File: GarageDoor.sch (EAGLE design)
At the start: 18 parts

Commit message: I hate git
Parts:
- added IC1: 7805DT, linear:7805DT
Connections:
- net GND: now also IC1.GND
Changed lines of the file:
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@@
 <part name="P+2" library="supply1" deviceset="+5V" device=""/>
 <part name="SUPPLY6" library="supply2" deviceset="GND" device=""/>
+<part name="SUPPLY7" library="supply2" deviceset="GND" device=""/>
+<part name="IC1" library="linear" deviceset="78*" device="DT" technology="05"/>
 </parts>
 <sheets>
@@
 <instance part="P+2" gate="1" x="213.36" y="38.1"/>
 <instance part="SUPPLY6" gate="GND" x="213.36" y="17.78"/>
+<instance part="SUPPLY7" gate="GND" x="-109.22" y="35.56"/>
+<instance part="IC1" gate="A1" x="-109.22" y="50.8"/>
 </instances>
 <busses>
@@
 <wire x1="213.36" y1="25.4" x2="213.36" y2="20.32" width="0.1524" layer="91"/>
 </segment>
+<segment>
+<pinref part="SUPPLY7" gate="GND" pin="GND"/>
+<wire x1="-109.22" y1="38.1" x2="-109.22" y2="43.18" width="0.1524" layer="91"/>
+<pinref part="IC1" gate="A1" pin="GND"/>
+</segment>
 </net>

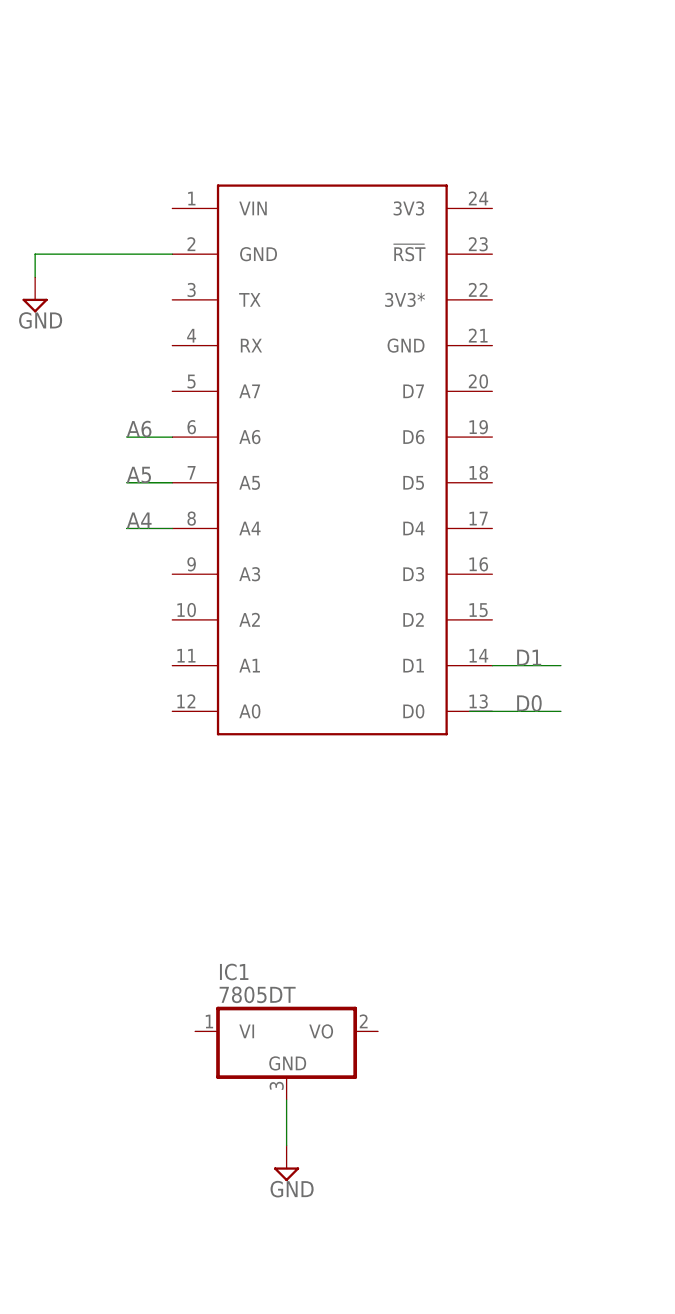
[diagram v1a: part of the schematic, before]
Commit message: 5V Regulator
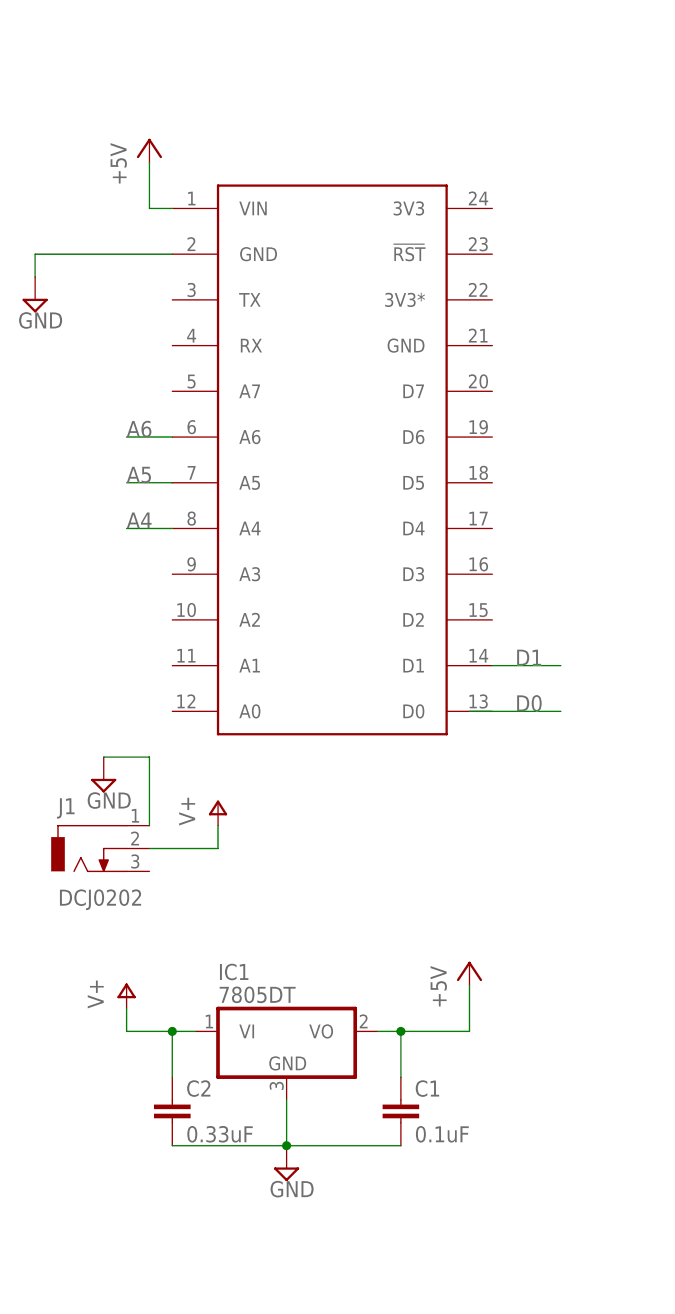
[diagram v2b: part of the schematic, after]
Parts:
- added C1: 0.1uF, rcl:C-EUC0805K
- added C2: 0.33uF, rcl:C-EUC0805K
- added J1: DCJ0202, con-jack:DCJ0202
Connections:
- new net V+: C2.1, IC1.VI, J1.2
- net +5V: now also C1.1, IC1.VO, U$1.VIN
- net GND: now also C1.2, C2.2, J1.1
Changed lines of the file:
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@@
 <part name="SUPPLY7" library="supply2" deviceset="GND" device=""/>
 <part name="IC1" library="linear" deviceset="78*" device="DT" technology="05"/>
+<part name="C1" library="rcl" deviceset="C-EU" device="C0805K" value="0.1uF"/>
+<part name="C2" library="rcl" deviceset="C-EU" device="C0805K" value="0.33uF"/>
+<part name="P+3" library="supply1" deviceset="+5V" device=""/>
+<part name="P+4" library="supply1" deviceset="+5V" device=""/>
+<part name="J1" library="con-jack" deviceset="DCJ0202" device=""/>
+<part name="P+5" library="supply1" deviceset="V+" device=""/>
+<part name="P+6" library="supply1" deviceset="V+" device=""/>
+<part name="SUPPLY8" library="supply2" deviceset="GND" device=""/>
 </parts>
 <sheets>
@@
 <instance part="SUPPLY7" gate="GND" x="-109.22" y="35.56"/>
 <instance part="IC1" gate="A1" x="-109.22" y="50.8"/>
+<instance part="C1" gate="G$1" x="-96.52" y="43.18"/>
+<instance part="C2" gate="G$1" x="-121.92" y="43.18"/>
+<instance part="P+3" gate="1" x="-124.46" y="149.86"/>
+<instance part="P+4" gate="1" x="-88.9" y="58.42"/>
+<instance part="J1" gate="G$1" x="-132.08" y="71.12"/>
+<instance part="P+5" gate="1" x="-116.84" y="76.2"/>
+<instance part="P+6" gate="1" x="-127" y="55.88"/>
+<instance part="SUPPLY8" gate="GND" x="-129.54" y="78.74"/>
 </instances>
 <busses>
@@
 <wire x1="-109.22" y1="38.1" x2="-109.22" y2="43.18" width="0.1524" layer="91"/>
 <pinref part="IC1" gate="A1" pin="GND"/>
+<pinref part="C2" gate="G$1" pin="2"/>
+<wire x1="-109.22" y1="38.1" x2="-121.92" y2="38.1" width="0.1524" layer="91"/>
+<junction x="-109.22" y="38.1"/>
+<pinref part="C1" gate="G$1" pin="2"/>
+<wire x1="-96.52" y1="38.1" x2="-109.22" y2="38.1" width="0.1524" layer="91"/>
+</segment>
+<segment>
+<pinref part="J1" gate="G$1" pin="1"/>
+<wire x1="-124.46" y1="73.66" x2="-124.46" y2="81.28" width="0.1524" layer="91"/>
+<pinref part="SUPPLY8" gate="GND" pin="GND"/>
+<wire x1="-124.46" y1="81.28" x2="-129.54" y2="81.28" width="0.1524" layer="91"/>
 </segment>
 </net>
@@
 <wire x1="213.36" y1="33.02" x2="213.36" y2="35.56" width="0.1524" layer="91"/>
 </segment>
+<segment>
+<pinref part="U$1" gate="G$1" pin="VIN"/>
+<wire x1="-121.92" y1="142.24" x2="-124.46" y2="142.24" width="0.1524" layer="91"/>
+<pinref part="P+3" gate="1" pin="+5V"/>
+<wire x1="-124.46" y1="142.24" x2="-124.46" y2="147.32" width="0.1524" layer="91"/>
+</segment>
+<segment>
+<pinref part="P+4" gate="1" pin="+5V"/>
+<wire x1="-88.9" y1="55.88" x2="-88.9" y2="50.8" width="0.1524" layer="91"/>
+<pinref part="C1" gate="G$1" pin="1"/>
+<wire x1="-96.52" y1="45.72" x2="-96.52" y2="50.8" width="0.1524" layer="91"/>
+<pinref part="IC1" gate="A1" pin="VO"/>
+<wire x1="-96.52" y1="50.8" x2="-99.06" y2="50.8" width="0.1524" layer="91"/>
+<junction x="-96.52" y="50.8"/>
+<wire x1="-96.52" y1="50.8" x2="-88.9" y2="50.8" width="0.1524" layer="91"/>
+</segment>
 </net>
 <net name="A4" class="0">
@@
 </segment>
 </net>
+<net name="V+" class="0">
+<segment>
+<pinref part="IC1" gate="A1" pin="VI"/>
+<wire x1="-119.38" y1="50.8" x2="-121.92" y2="50.8" width="0.1524" layer="91"/>
+<pinref part="C2" gate="G$1" pin="1"/>
+<wire x1="-121.92" y1="45.72" x2="-121.92" y2="50.8" width="0.1524" layer="91"/>
+<junction x="-121.92" y="50.8"/>
+<wire x1="-121.92" y1="50.8" x2="-127" y2="50.8" width="0.1524" layer="91"/>
+<pinref part="P+6" gate="1" pin="V+"/>
+<wire x1="-127" y1="50.8" x2="-127" y2="53.34" width="0.1524" layer="91"/>
+</segment>
+<segment>
+<pinref part="J1" gate="G$1" pin="2"/>
+<pinref part="P+5" gate="1" pin="V+"/>
+<wire x1="-124.46" y1="71.12" x2="-116.84" y2="71.12" width="0.1524" layer="91"/>
+<wire x1="-116.84" y1="71.12" x2="-116.84" y2="73.66" width="0.1524" layer="91"/>
+</segment>
+</net>

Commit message: Hall Effect Circuitry
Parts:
- added R12, R13: 1K, resistor:R-US_R0805
- added R14, R15: 10K, resistor:R-US_R0805
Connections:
- new net D3: R12.1, U$1.D3
- new net D4: R13.1, U$1.D4
- new net N$13: HALL_CONN.2, R12.2, R14.1
- new net N$15: HALL_CONN.3, R13.2, R15.1
- net +5V: now also R14.2, R15.2
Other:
- note added: "D3 Is the Closed Detector D4 is the Opened Detector"
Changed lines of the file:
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@@
 <part name="P+6" library="supply1" deviceset="V+" device=""/>
 <part name="SUPPLY8" library="supply2" deviceset="GND" device=""/>
+<part name="R12" library="resistor" deviceset="R-US_" device="R0805" value="1K"/>
+<part name="R13" library="resistor" deviceset="R-US_" device="R0805" value="1K"/>
+<part name="R15" library="resistor" deviceset="R-US_" device="R0805" value="10K"/>
+<part name="R14" library="resistor" deviceset="R-US_" device="R0805" value="10K"/>
+<part name="P+7" library="supply1" deviceset="+5V" device=""/>
+<part name="P+8" library="supply1" deviceset="+5V" device=""/>
 </parts>
 <sheets>
@@
 <text x="233.68" y="27.94" size="1.778" layer="91">Hall Effect Switches Header</text>
 <text x="228.6" y="152.4" size="1.778" layer="91">RGB Led Subsystem</text>
+<text x="233.68" y="20.32" size="1.778" layer="91">D3 Is the Closed Detector
+D4 is the Opened Detector</text>
 </plain>
 <instances>
@@
 <instance part="P+6" gate="1" x="-127" y="55.88"/>
 <instance part="SUPPLY8" gate="GND" x="-129.54" y="78.74"/>
+<instance part="R12" gate="G$1" x="193.04" y="35.56"/>
+<instance part="R13" gate="G$1" x="193.04" y="5.08"/>
+<instance part="R15" gate="G$1" x="203.2" y="12.7" rot="R90"/>
+<instance part="R14" gate="G$1" x="205.74" y="43.18" rot="R90"/>
+<instance part="P+7" gate="1" x="205.74" y="53.34"/>
+<instance part="P+8" gate="1" x="203.2" y="22.86"/>
 </instances>
 <busses>
@@
 <wire x1="-96.52" y1="50.8" x2="-88.9" y2="50.8" width="0.1524" layer="91"/>
 </segment>
+<segment>
+<pinref part="R14" gate="G$1" pin="2"/>
+<pinref part="P+7" gate="1" pin="+5V"/>
+<wire x1="205.74" y1="48.26" x2="205.74" y2="50.8" width="0.1524" layer="91"/>
+</segment>
+<segment>
+<pinref part="R15" gate="G$1" pin="2"/>
+<pinref part="P+8" gate="1" pin="+5V"/>
+<wire x1="203.2" y1="17.78" x2="203.2" y2="20.32" width="0.1524" layer="91"/>
+</segment>
 </net>
 <net name="A4" class="0">
@@
 <label x="-83.82" y="86.36" size="1.778" layer="95"/>
 </segment>
-<segment>
-<wire x1="223.52" y1="30.48" x2="213.36" y2="30.48" width="0.1524" layer="91"/>
-<label x="215.9" y="30.48" size="1.778" layer="95"/>
-</segment>
 </net>
 <net name="D1" class="0">
@@
 <wire x1="-86.36" y1="91.44" x2="-78.74" y2="91.44" width="0.1524" layer="91"/>
 <label x="-83.82" y="91.44" size="1.778" layer="95"/>
-</segment>
-<segment>
-<wire x1="223.52" y1="27.94" x2="213.36" y2="27.94" width="0.1524" layer="91"/>
-<label x="215.9" y="27.94" size="1.778" layer="95"/>
 </segment>
 </net>
@@
 </segment>
 </net>
+<net name="D3" class="0">
+<segment>
+<pinref part="U$1" gate="G$1" pin="D3"/>
+<wire x1="-86.36" y1="101.6" x2="-78.74" y2="101.6" width="0.1524" layer="91"/>
+<label x="-83.82" y="101.6" size="1.778" layer="95"/>
+</segment>
+<segment>
+<pinref part="R12" gate="G$1" pin="1"/>
+<wire x1="187.96" y1="35.56" x2="182.88" y2="35.56" width="0.1524" layer="91"/>
+<label x="182.88" y="35.56" size="1.778" layer="95"/>
+</segment>
+</net>
+<net name="D4" class="0">
+<segment>
+<pinref part="U$1" gate="G$1" pin="D4"/>
+<wire x1="-86.36" y1="106.68" x2="-78.74" y2="106.68" width="0.1524" layer="91"/>
+<label x="-83.82" y="106.68" size="1.778" layer="95"/>
+</segment>
+<segment>
+<pinref part="R13" gate="G$1" pin="1"/>
+<wire x1="187.96" y1="5.08" x2="182.88" y2="5.08" width="0.1524" layer="91"/>
+<label x="182.88" y="5.08" size="1.778" layer="95"/>
+</segment>
+</net>
+<net name="N$13" class="0">
+<segment>
+<pinref part="HALL_CONN" gate="1" pin="2"/>
+<wire x1="220.98" y1="30.48" x2="205.74" y2="30.48" width="0.1524" layer="91"/>
+<wire x1="205.74" y1="30.48" x2="205.74" y2="35.56" width="0.1524" layer="91"/>
+<pinref part="R12" gate="G$1" pin="2"/>
+<wire x1="205.74" y1="35.56" x2="198.12" y2="35.56" width="0.1524" layer="91"/>
+<pinref part="R14" gate="G$1" pin="1"/>
+<wire x1="205.74" y1="35.56" x2="205.74" y2="38.1" width="0.1524" layer="91"/>
+<junction x="205.74" y="35.56"/>
+</segment>
+</net>
+<net name="N$15" class="0">
+<segment>
+<pinref part="HALL_CONN" gate="1" pin="3"/>
+<wire x1="220.98" y1="27.94" x2="208.28" y2="27.94" width="0.1524" layer="91"/>
+<wire x1="208.28" y1="27.94" x2="208.28" y2="5.08" width="0.1524" layer="91"/>
+<pinref part="R13" gate="G$1" pin="2"/>
+<wire x1="208.28" y1="5.08" x2="203.2" y2="5.08" width="0.1524" layer="91"/>
+<pinref part="R15" gate="G$1" pin="1"/>
+<wire x1="203.2" y1="5.08" x2="198.12" y2="5.08" width="0.1524" layer="91"/>
+<wire x1="203.2" y1="5.08" x2="203.2" y2="7.62" width="0.1524" layer="91"/>
+<junction x="203.2" y="5.08"/>
+</segment>
+</net>
 </nets>
 </sheet>
@@
 </schematic>
 </drawing>
+<compatibility>
+<note version="6.3" minversion="6.2.2" severity="warning">
+Since Version 6.2.2 text objects can contain more than one line,
+which will not be processed correctly with this version.
+</note>
+</compatibility>
 </eagle>
